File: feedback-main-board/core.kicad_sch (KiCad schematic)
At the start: 38 parts, among them SW1 SW_SPDT, SW2 SW_SPDT, U1 TL074, U2 TL074

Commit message: rev4
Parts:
- C10, C11: LCSC (none) -> C1634
- C12, C13, C5, C6, C7, C8, C9, D2, D3, D4, D5, RV1, RV2, RV3, SW1, SW2: LCSC (none) -> DNP
- C14, C15: LCSC (none) -> C14663; Mouser (none) -> 581-06035C105MAT2A
- R10, R11, R18, R19, R9: LCSC (none) -> C22775
- R12, R13, R14, R20: LCSC (none) -> C25804
- R15, R16, R17, R6, R8: LCSC (none) -> C25803
- R5, R7: LCSC (none) -> C22935
- U1, U2: value TL074 -> OPA1679; LCSC (none) -> C2878631; Mouser 595-TL074IDR -> (none)
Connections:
- net Feedback: no longer SW2.3 (C)
- net PreFeedback: now reaches C13.2, RV3.3
- net PreFeedback: now also SW2.3 (C)

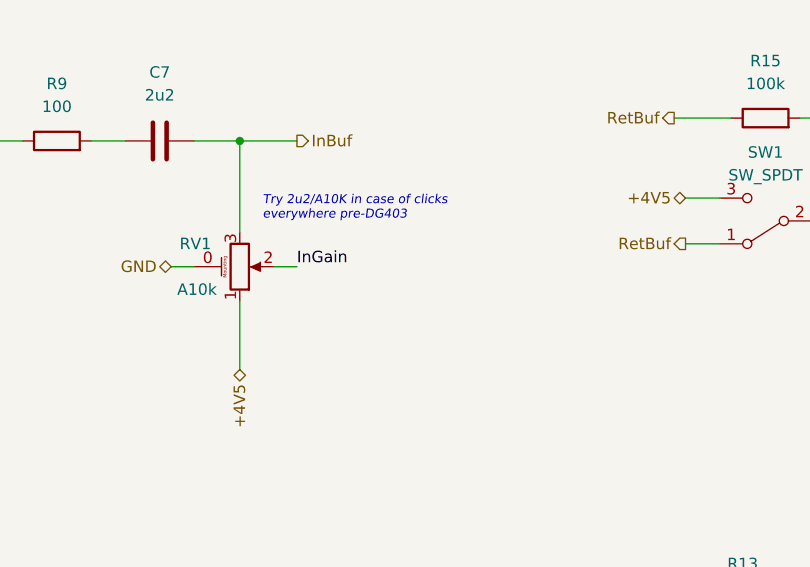
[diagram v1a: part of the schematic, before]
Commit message: Added note about larger pots
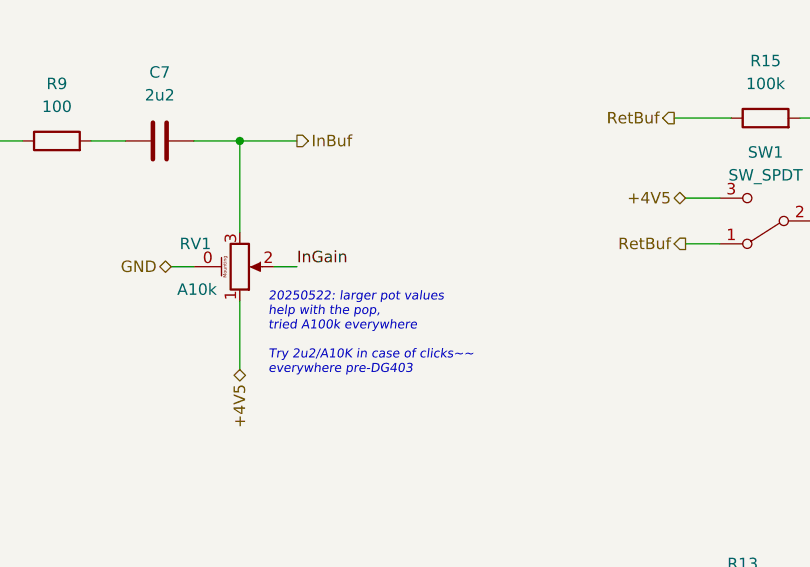
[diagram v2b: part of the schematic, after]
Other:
- note added: "20250522: larger pot values help with the pop, tried A100k everywhere Try 2u2/A10K in case of clicks~~ everywhere pre-DG403"
- note removed: "Try 2u2/A10K in case of clicks everywhere pre-DG403"
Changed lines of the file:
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@@
     (effects (font (size 1 1) italic) (justify left bottom))
   )
-  (text "Try 2u2/A10K in case of clicks\neverywhere pre-DG403"
-    (at 96.52 57.15 0)
+  (text "20250522: larger pot values\nhelp with the pop,\ntried A100k everywhere\n\nTry 2u2/A10K in case of clicks~~\neverywhere pre-DG403"
+    (at 97.155 74.295 0)
     (effects (font (size 1 1) italic) (justify left bottom))
   )
